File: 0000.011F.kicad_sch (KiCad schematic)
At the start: 43 parts, among them J1 XH, J2 XH, J3 XH, J4 XH, J5 XH, J6 XH, J7 XH, J8 XH, J9 XH, U1 TL071, U2 TL071, U3 TL072

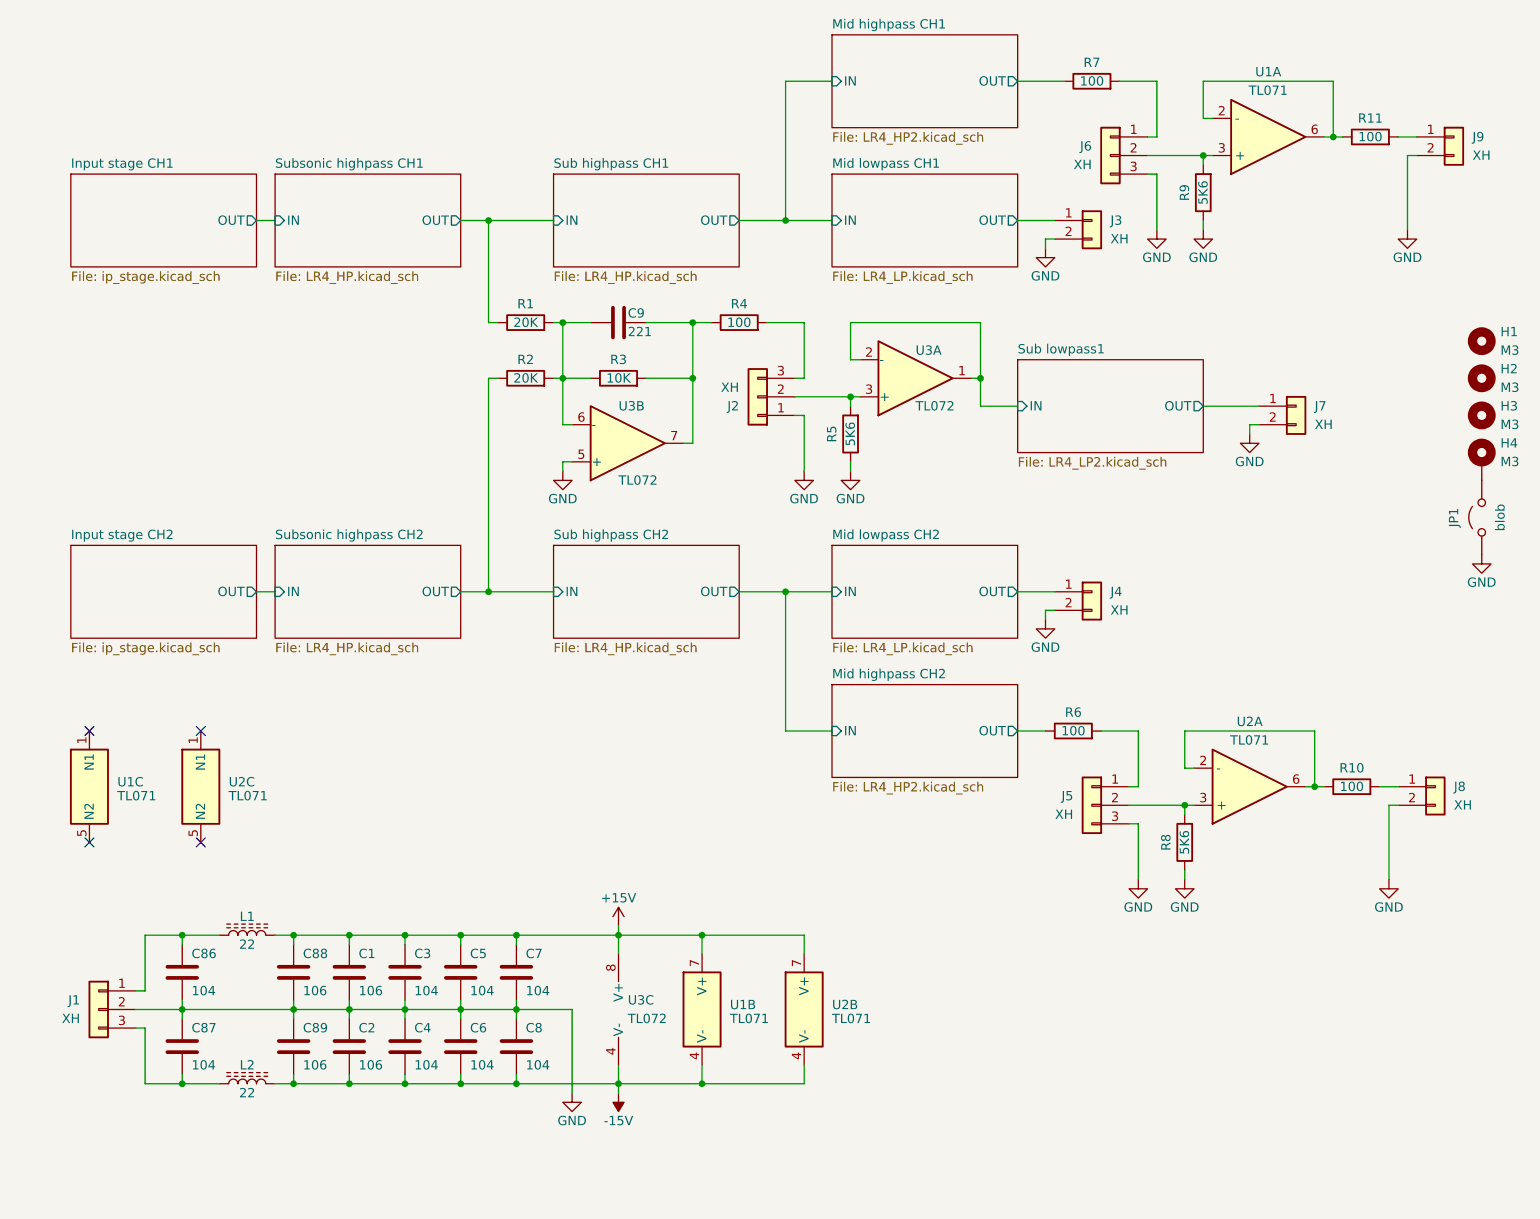
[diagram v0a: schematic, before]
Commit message: Added XLR input connectors for direct panel mounting. Added snap-off board for the level control pots with ribbon cable connection to the main board.
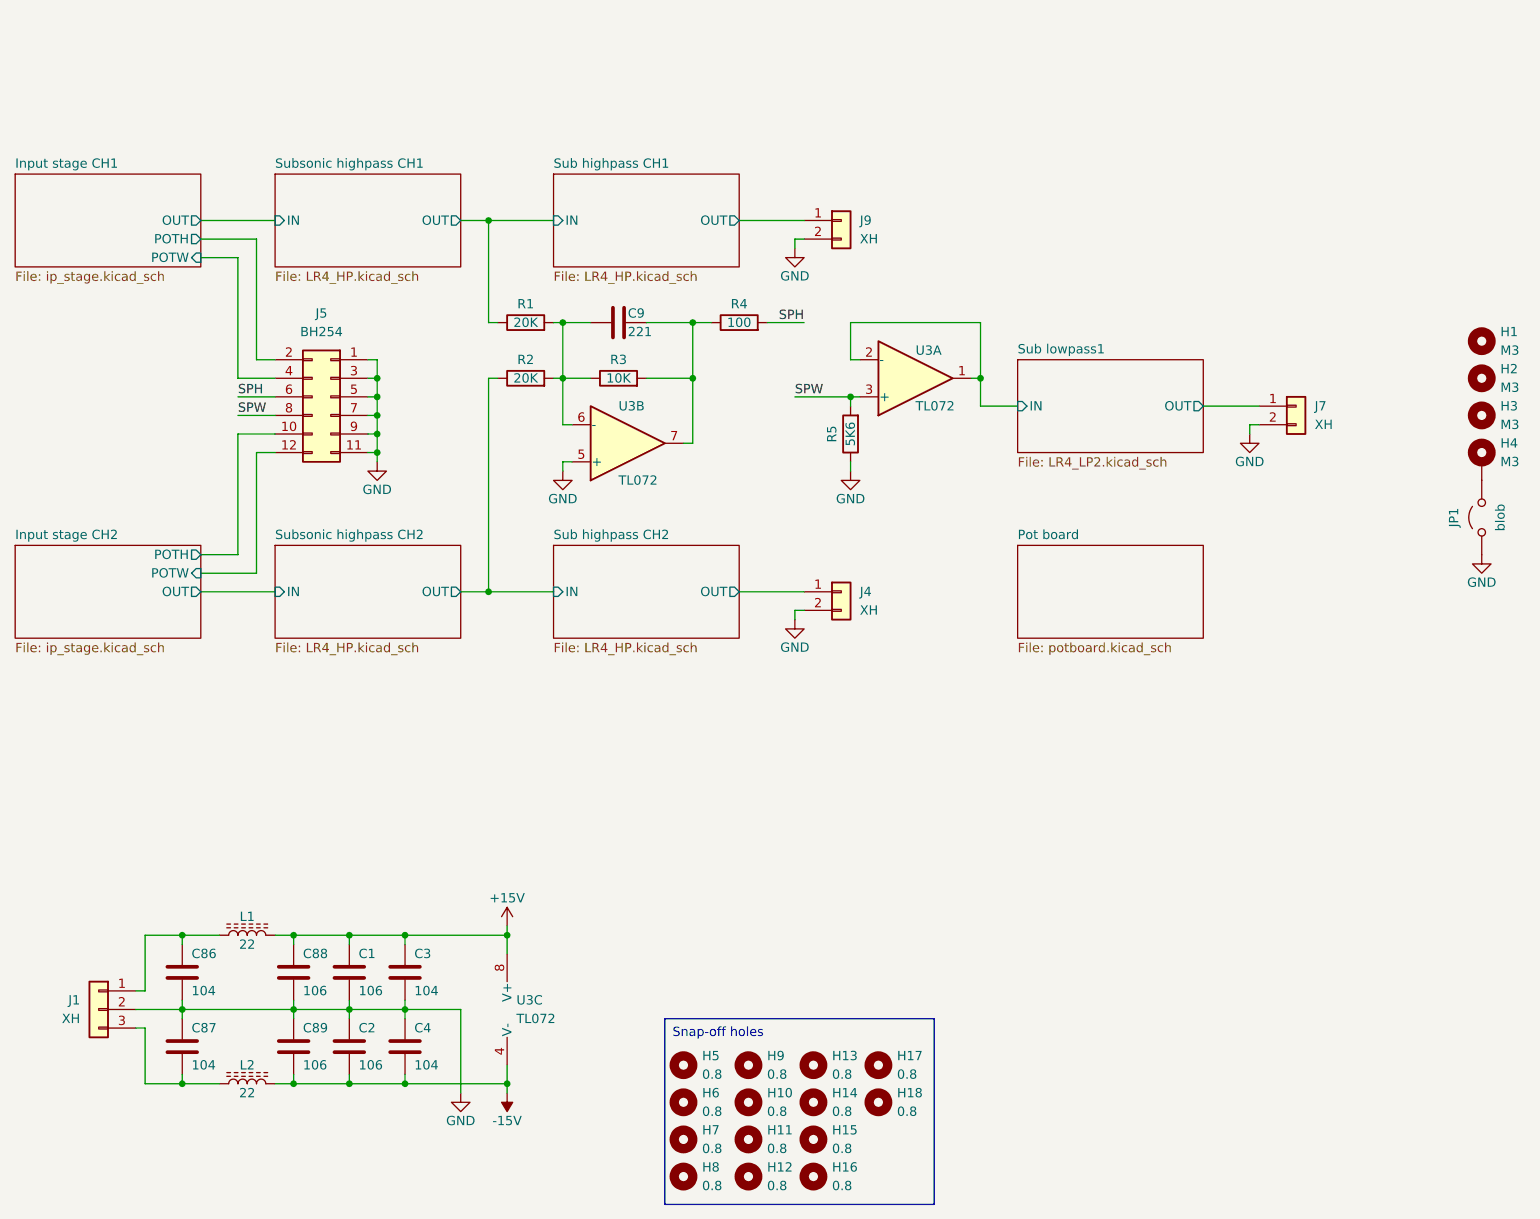
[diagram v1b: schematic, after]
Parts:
- removed C5, C6, C7, C8: 104, Capacitor_SMD:C_0805_2012Metric, symbol Device:C
- removed J2, J5, J6: XH, Connector_JST:JST_XH_B3B-XH-AM_1x03_P2.50mm_Vertical, symbol Connector_Generic:Conn_01x03
- removed J3, J8: XH, Connector_JST:JST_XH_B2B-XH-AM_1x02_P2.50mm_Vertical, symbol Connector_Generic:Conn_01x02
- removed R10, R11, R6, R7: 100, Resistor_SMD:R_0805_2012Metric, symbol Device:R
- removed R8, R9: 5K6, Resistor_SMD:R_0805_2012Metric, symbol Device:R
- removed U1, U2: TL071, Package_SO:SOIC-8_3.9x4.9mm_P1.27mm, symbol HR Parts:OPAMP_GENERIC_8P_MP
- added H10, H11, H12, H13, H14, H15, H16, H17, H18, H5, H6, H7, H8, H9: 0.8, HR_Parts:HOLE_0.8, symbol Mechanical:MountingHole
- added J5: BH254, Connector_IDC:IDC-Header_2x06_P2.54mm_Vertical, symbol Connector_Generic:Conn_02x06_Odd_Even
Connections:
- net GND: now also J5.1 (Pin_1), J5.11 (Pin_11), J5.3 (Pin_3), J5.5 (Pin_5), J5.7 (Pin_7), J5.9 (Pin_9)
- net Sub highpass CH1/OUT: now reaches J9.1 (Pin_1)
- net SPW: now reaches R5.2, U3.3 (+)
- net SPW: now also J5.8 (Pin_8)
- net SPH: now reaches R4.2
- net SPH: now also J5.6 (Pin_6)
- net Mid lowpass CH2/OUT renamed Sub highpass CH2/OUT
- new net Input stage CH1/POTH: J5.2 (Pin_2)
- new net Input stage CH1/POTW: J5.4 (Pin_4)
- new net Input stage CH2/POTH: J5.10 (Pin_10)
- new net Input stage CH2/POTW: J5.12 (Pin_12)
- no-connect marks 4 -> 0
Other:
- removed sheet Mid highpass CH1
- removed sheet Mid highpass CH2
- removed sheet Mid lowpass CH1
- removed sheet Mid lowpass CH2
- added sheet Pot board (potboard.kicad_sch)
- sheet Input stage CH1 ports: added POTH, POTW; removed none
- sheet Input stage CH2 ports: added POTH, POTW; removed none
- moved on the sheet: J4, J9, U3C
